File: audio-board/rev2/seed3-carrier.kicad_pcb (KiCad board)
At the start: 4 copper layers, 90 x 56.5 mm, 54 parts, among them J1 NRJ4HF, J2 SJ3-35063AG, J3 DISPLAY_UART, J4 SJ3-35063AG, J5 SPEAKER_SEND, J6 POWER_BOARD, Q1 AO3401A, Q2 2N7002, U1 TLV9061IDBVR, U2 TPA6132A2RTE

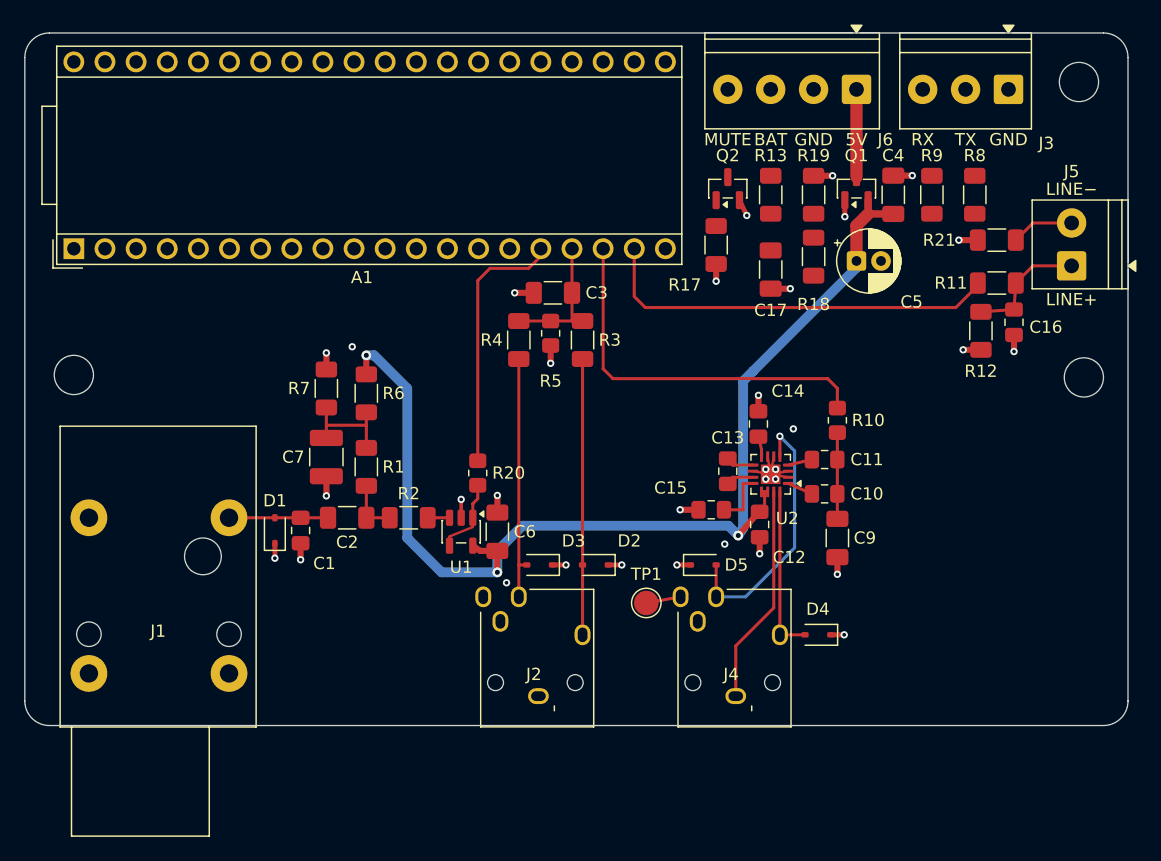
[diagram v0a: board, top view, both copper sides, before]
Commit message: Align the jack noses and rework mounting holes; add fiducials
J1 moves 5.9 mm back so its nose tip ends on the same line as J2's and
J4's. The guitar input row, U1 and the VREF block move with it, and the
analog +5V branch on L4 is re-routed to C6 and R6.

Mounting holes become three M2.5: H2 rear-right and H3 front-right, 4 mm
in from the edges, and H1 rear-left in the 6.4 mm gap behind J1, where an
M3's keep-out doesn't fit. J1's nut still holds the front-left corner.
Three asymmetric 1 mm fiducials go next to the holes for JLC's assembly
camera. Holes and fiducials are board-only footprints.

Co-Authored-By: Claude Opus 5.5 <noreply@anthropic.com>
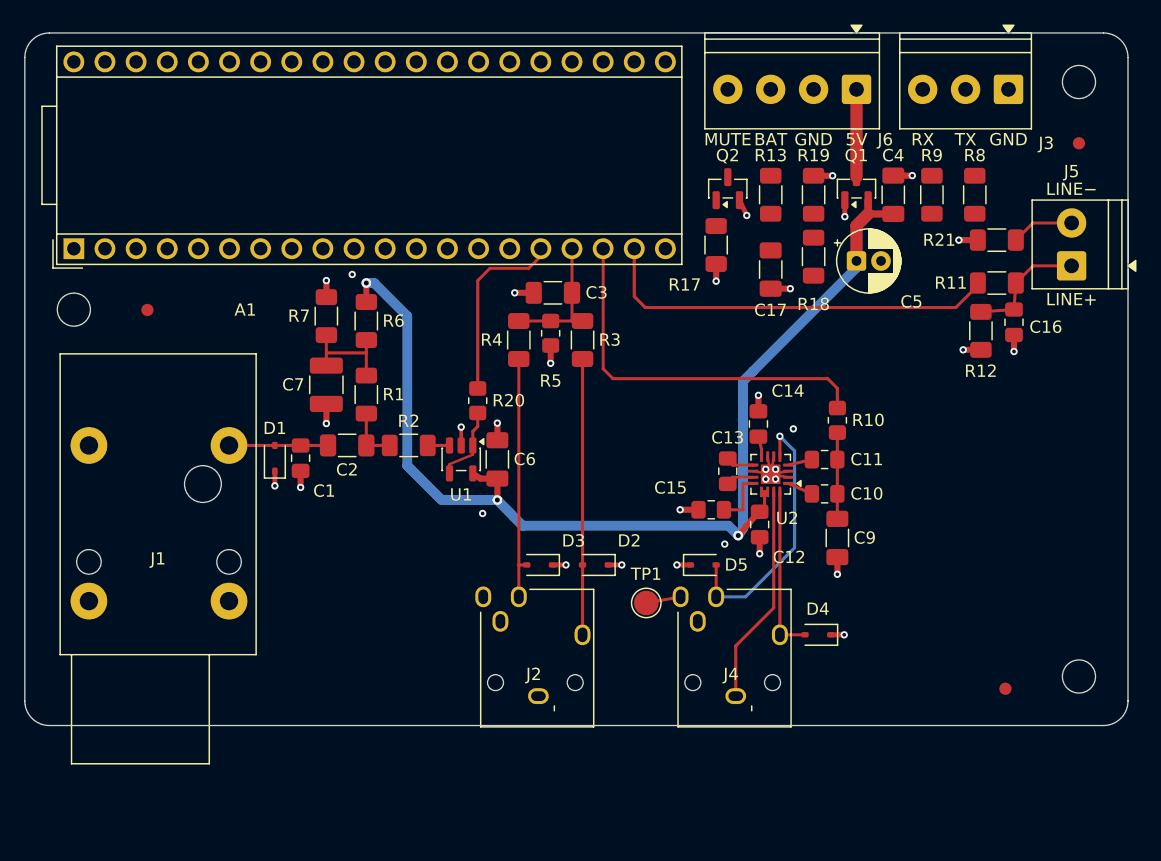
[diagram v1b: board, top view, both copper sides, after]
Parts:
- added FID1: Fiducial, Fiducial:Fiducial_1mm_Mask2mm, F.Cu at (110.0, 72.6)
- added FID2: Fiducial, Fiducial:Fiducial_1mm_Mask2mm, F.Cu at (186.0, 59.0)
- added FID3: Fiducial, Fiducial:Fiducial_1mm_Mask2mm, F.Cu at (180.0, 103.5)
- H1, H2, H3: value MountingHole_3.2mm_M3 -> MountingHole_2.7mm_M2.5; footprint MountingHole:MountingHole_3.2mm_M3 -> MountingHole:MountingHole_2.7mm_M2.5
- moved H3 24.4 mm to (186.0, 102.5)
- moved C1 5.90 mm to (122.5, 84.7)
- moved R1 5.90 mm to (127.9, 79.5)
- moved R6 5.90 mm to (127.9, 73.5)
- moved R7 5.90 mm to (124.6, 73.1)
- moved C2 5.90 mm to (126.3, 83.7)
- moved C6 5.90 mm to (138.5, 84.8)
- moved C7 5.90 mm to (124.6, 78.7)
- moved D1 5.90 mm to (120.4, 84.7)
- moved J1 5.90 mm to (116.7, 83.7)
- moved R2 5.90 mm to (131.3, 83.7)
- moved R20 5.90 mm to (136.9, 80.0)
- moved U1 5.90 mm to (135.6, 84.8)
- moved H1 5.33 mm to (104.0, 72.6)
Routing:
- net /AUDIO_IN_1: track 21.3 -> 15.4 mm
- net +5V: track 91.0 -> 89.3 mm

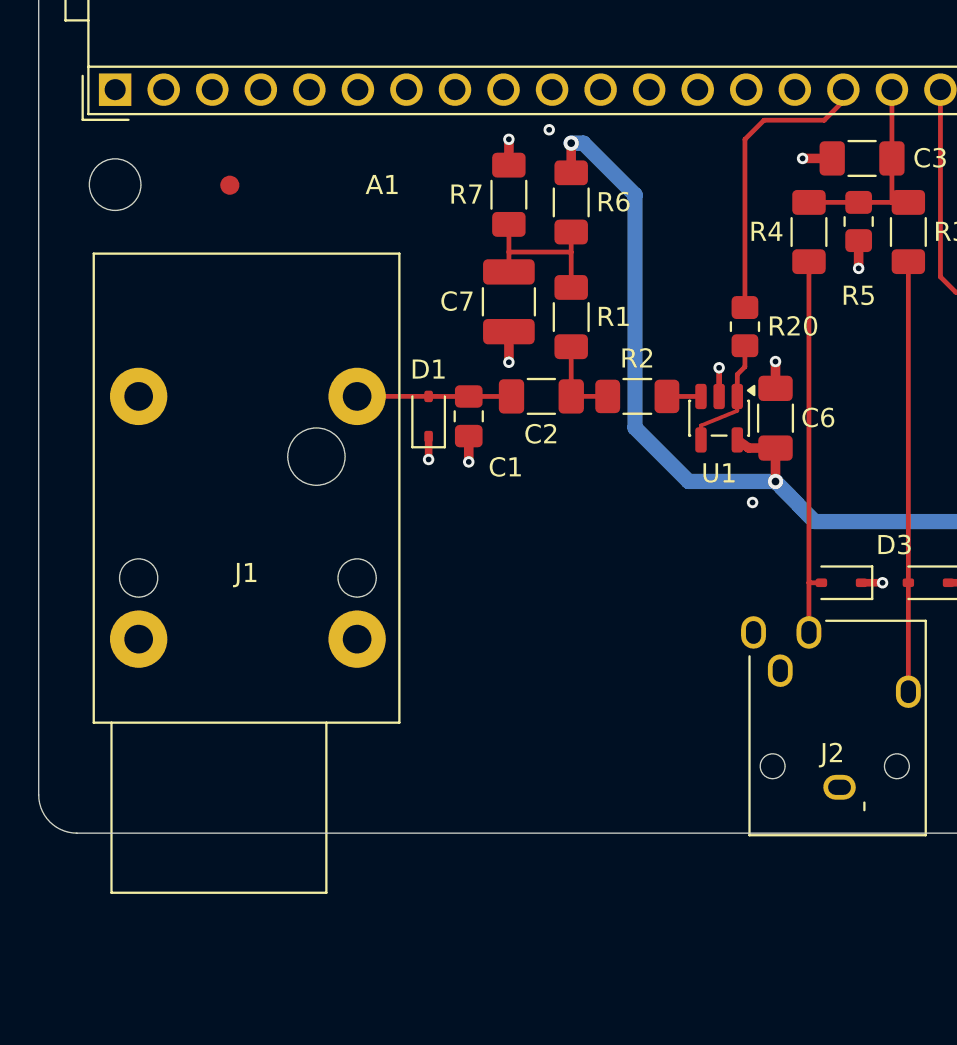
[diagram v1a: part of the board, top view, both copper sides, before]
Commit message: Put J1 back with all jack faces on the board edge
Aligning the nose tips was wrong: the Neutrik NRJ4HF is rear-mounted, so
its face has to press on the back of the panel like the SJ3 faces, with
its 8.9 mm threaded nose through the panel for the nut (Neutrik drawing
ST-NRJ4HF). J1, the guitar input section and the analog +5V branch go
back to where they were before 771cb61.

Kept from 771cb61: three M2.5 mounting holes (H1 back in its original
spot behind J1, H2 rear-right, H3 front-right) and the three fiducials.
Both jack footprints were checked against the manufacturers' drawings.

Co-Authored-By: Claude Opus 5.5 <noreply@anthropic.com>
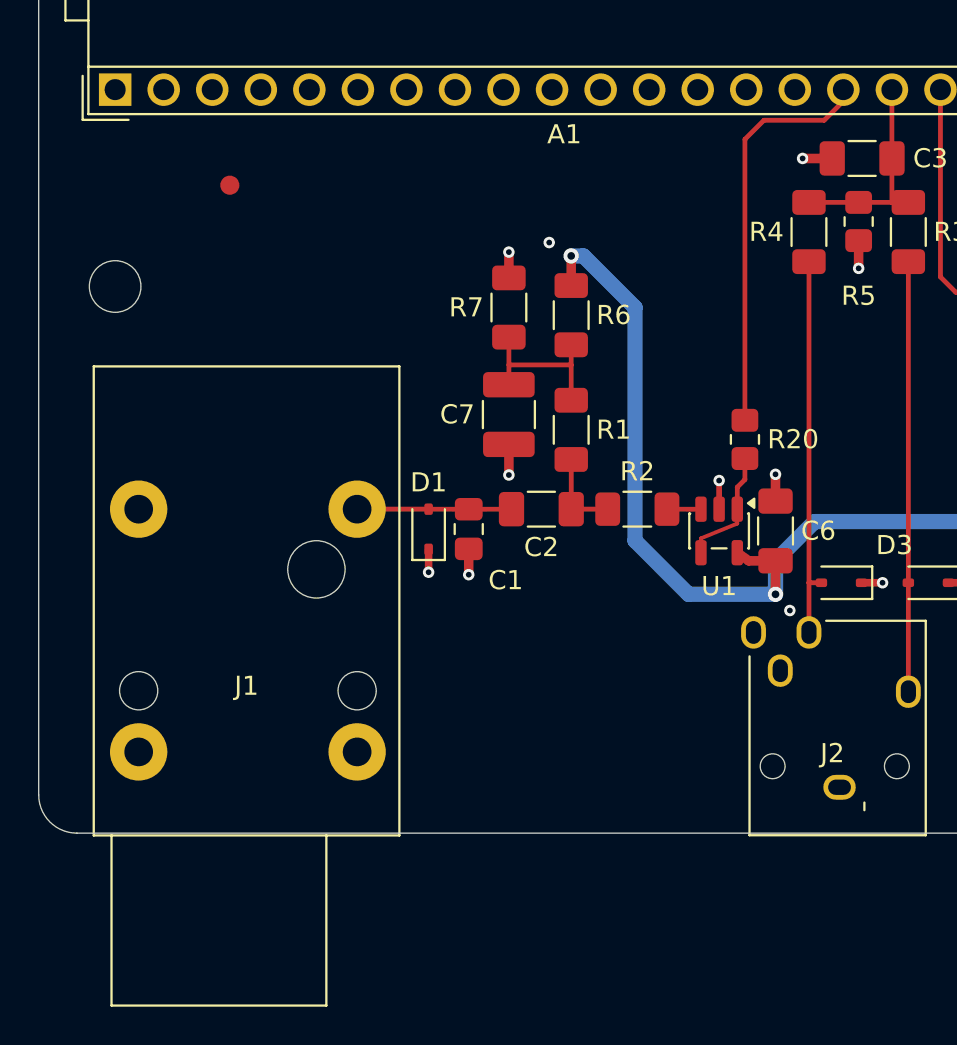
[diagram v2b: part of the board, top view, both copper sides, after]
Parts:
- moved C1 5.90 mm to (122.5, 90.6)
- moved R1 5.90 mm to (127.9, 85.4)
- moved R6 5.90 mm to (127.9, 79.4)
- moved R7 5.90 mm to (124.6, 79.0)
- moved C2 5.90 mm to (126.3, 89.5)
- moved C6 5.90 mm to (138.5, 90.7)
- moved C7 5.90 mm to (124.6, 84.6)
- moved D1 5.90 mm to (120.4, 90.6)
- moved J1 5.90 mm to (116.7, 89.5)
- moved R2 5.90 mm to (131.3, 89.5)
- moved R20 5.90 mm to (136.9, 85.9)
- moved U1 5.90 mm to (135.6, 90.7)
- moved H1 5.33 mm to (104.0, 77.9)
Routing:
- net /AUDIO_IN_1: track 15.4 -> 21.3 mm
- net +5V: track 89.3 -> 91.0 mm

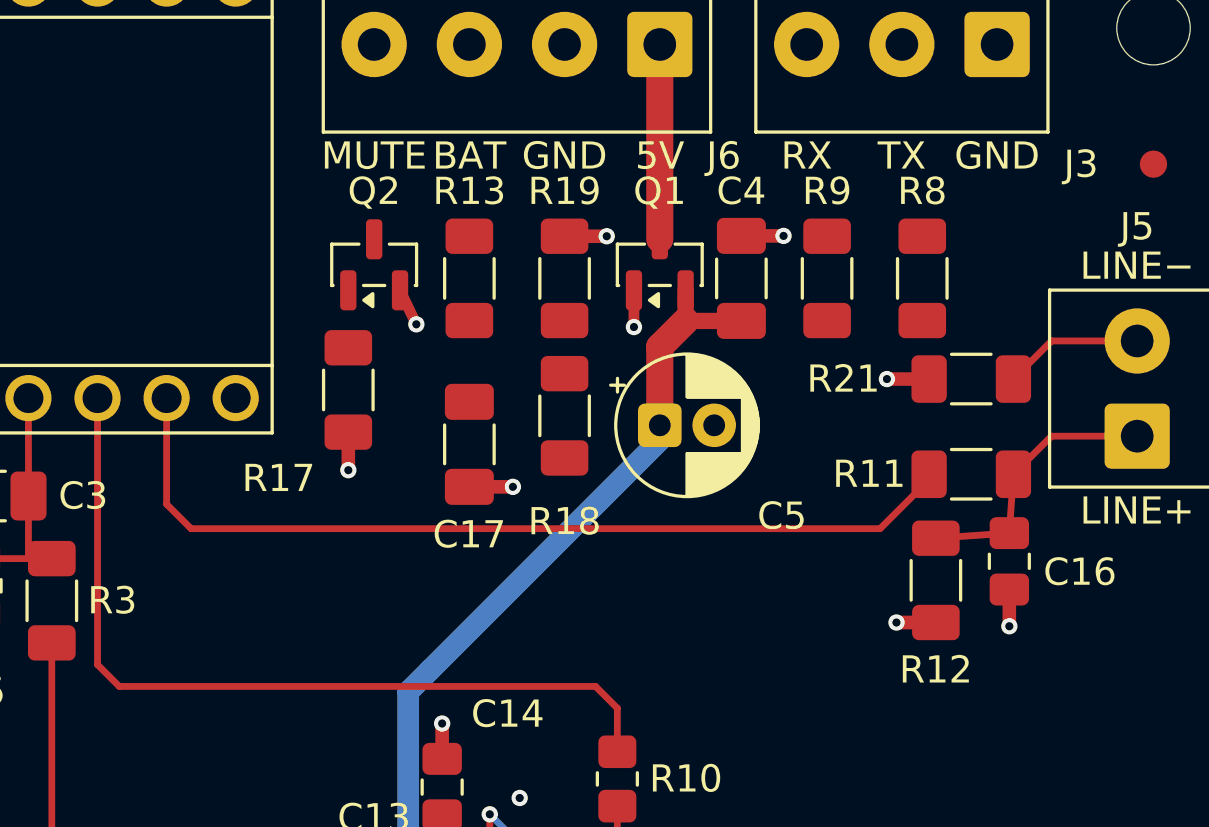
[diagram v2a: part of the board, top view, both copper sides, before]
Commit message: Fix the carrier's circuit-check failures: wrong-terminal 5 V and AUX into an off codec
The first run of tools/kicad/circuit_verify.py on the carrier failed five ways. Each is fixed in the
circuit, with no waivers:

- R22 (10k, BATT_SENSE to GND): R13/R22 halve BAT. A 5 V wire on BAT now puts at most 2.65 V on pin 25
  (PA7, a TT_a pin: 4.0 V max, no positive injection), and a full 3.3 V battery reading (1.65 V) stays
  inside the ADC's range.
- R23 (470 ohm, J6.4 to Q2's drain): a 5 V wire on MUTE with Q2 on now draws 11 mA instead of 0.75-2.5 A
  through a 115 mA part.
- R24 (100k, DISPLAY_UART_RX to GND): with R9 it divides a 5 V wire on RX to 4.78 V (Seed3 GPIO 0-5 V).
  An unplugged display now reads as a held-low line, which the firmware can use to detect it.
- R5 3.3k -> 470 ohm: a source left playing into J2 with the board off now reaches the unpowered
  codec's input at +/-0.23 V, inside its +/-0.3 V rating (was +/-0.8 V, ~0.5 mA into its diodes).
  The AUX input is ~11 dB quieter; the firmware adds the gain back.

Board: R23 tops the MUTE column (Q2 and R17 move down), R22 lies across the band below R18 and C5,
R24 sits under R9, and AUDIO_OUT_2's run under the corner moves from y = 72.4 to 76.3 to make room.
The new signal links stay unrouted with the rest of the corner.

The spec's AUX claims follow DESIGN.md's new levels. DESIGN.md, CHANGES.md and TEST_PLAN.md are updated,
including power-board requirements (BAT source <= 10k, SPK_MUTE pull-up >= 4.7k) and firmware notes.

Co-Authored-By: Claude Opus 5.5 <noreply@anthropic.com>
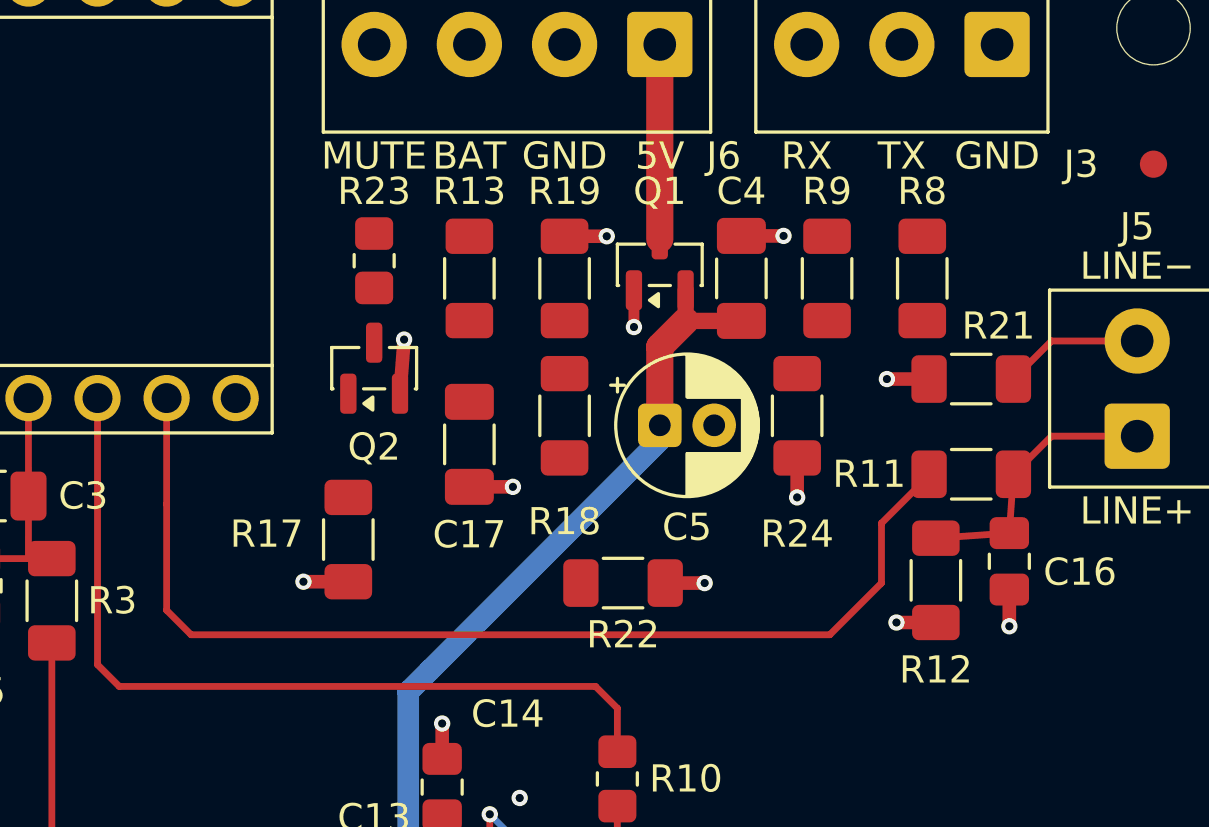
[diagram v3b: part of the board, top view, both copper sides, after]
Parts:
- added R22: 10k, Resistor_SMD:R_1206_3216Metric_Pad1.30x1.75mm_HandSolder, F.Cu at (166.5, 74.4)
- added R23: 470, Resistor_SMD:R_0805_2012Metric_Pad1.20x1.40mm_HandSolder, F.Cu at (157.3, 62.5)
- added R24: 100k, Resistor_SMD:R_1206_3216Metric_Pad1.30x1.75mm_HandSolder, F.Cu at (172.9, 68.2)
- R5: value 3.3k -> 470
- moved R17 5.50 mm to (156.4, 72.8)
- moved Q2 3.80 mm to (157.3, 66.5)
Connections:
- Q2 pad 3: /SPK_MUTE -> Net-(Q2-D)
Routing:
- net /AUDIO_OUT_2: track 33.2 -> 40.0 mm
- net GND: track 56.5 -> 60.3 mm, vias 33 -> 35

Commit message: Route the carrier's last 18 connections
The power board signals, display UART and Daisy VIN run in ordered lanes
on L4 between the Daisy's header rows. TX and RX drop to pins 14/15 on L1
past the VIN lane, and HP_DETECT hops to L4 under the two audio-out traces.
Each signal via has a GND return via beside it. The board check finds no
unrouted connections and no errors.

Co-Authored-By: Claude Opus 5.5 <noreply@anthropic.com>
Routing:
- net +5V: track 91.0 -> 170.3 mm
- net /DISPLAY_UART_TX: track 0.00 -> 48.7 mm, vias 0 -> 2
- net /HP_DETECT: track 2.84 -> 49.1 mm, vias 0 -> 2
- net /BATT_SENSE: track 0.00 -> 44.6 mm, vias 0 -> 1
- net /DISPLAY_UART_RX: track 0.00 -> 42.9 mm, vias 0 -> 2
- net /SPK_EN: track 0.00 -> 38.5 mm, vias 0 -> 1
- net /5V_SENSE: track 0.00 -> 26.6 mm, vias 0 -> 1
- net /UART_TX_CONN: track 0.00 -> 7.16 mm
- net /UART_RX_CONN: track 0.00 -> 7.16 mm
- net /BATT_SENSE_CONN: track 0.00 -> 7.05 mm
- net /SPK_MUTE: track 0.00 -> 6.95 mm
- net Net-(Q2-D): track 0.00 -> 2.01 mm
- net GND: vias 35 -> 43
